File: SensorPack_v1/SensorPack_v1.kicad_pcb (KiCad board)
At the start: 4 copper layers, 53.5 x 50 mm, 31 parts, among them J2 M12x5 A-Type, J3 2x3 Header, J4 M12x5 A-Type, Q1 DMN2310U, U1 STM32C092KCT6, U3 MCP2562-E-SN, U4 TLV7xx_SOT23-5, Y1 8MHz 16pF Load

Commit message: Featured out SensorPack_v1
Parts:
- removed C12: 100nF, Resistor_SMD:R_0603_1608Metric_Pad0.98x0.95mm_HandSolder
- removed C9: 10uF 16V, Capacitor_SMD:C_0805_2012Metric_Pad1.18x1.45mm_HandSolder
- removed D3: 12V TVS 1CH, Diode_SMD:D_SMA
- removed U4: TLV7xx_SOT23-5, Package_TO_SOT_SMD:SOT-23-5
- added C5: 100nF, Resistor_SMD:R_0603_1608Metric_Pad0.98x0.95mm_HandSolder, F.Cu at (132.8, 54.2)
- added C6: 10uF 16V, Capacitor_SMD:C_0805_2012Metric_Pad1.18x1.45mm_HandSolder, F.Cu at (131.8, 66.0)
- added D2: 12V TVS 1CH, Diode_SMD:D_SMA, F.Cu at (140.5, 54.2)
- added J1: M12x5 A-Type, Capstone_Footprints:M12x5_A_Circular_Connector, F.Cu at (148.5, 60.0)
- added J10: 2x3 Pogo Header, Capstone_Footprints:2x03_2.54mm_DIP_pogo, B.Cu at (102.5, 75.0)
- added J5: 4p Header, Connector_PinHeader_2.54mm:PinHeader_1x04_P2.54mm_Vertical, F.Cu at (118.5, 96.7)
- added J6: 4p Header, Connector_PinHeader_2.54mm:PinHeader_1x04_P2.54mm_Vertical, F.Cu at (111.5, 54.0)
- added J7: 4p Header, Connector_PinHeader_2.54mm:PinHeader_1x04_P2.54mm_Vertical, F.Cu at (111.0, 96.7)
- added J8: 6p Header, Connector_PinHeader_2.54mm:PinHeader_1x06_P2.54mm_Vertical, F.Cu at (104.0, 54.0)
- added J9: 4p Header, Connector_PinHeader_2.54mm:PinHeader_1x04_P2.54mm_Vertical, F.Cu at (104.0, 96.5)
- added JP1: Jumper_3_Bridged12, Capstone_Footprints:Jumper_0603_2pos, F.Cu at (128.5, 95.7)
- added JP2: Jumper_3_Bridged12, Capstone_Footprints:Jumper_0603_2pos, F.Cu at (121.0, 95.7)
- added JP3: Jumper_2_Small_Open, Resistor_SMD:R_0603_1608Metric_Pad0.98x0.95mm_HandSolder, F.Cu at (119.0, 64.2)
- added JP4: Jumper_3_Bridged12, Capstone_Footprints:Jumper_0603_2pos, F.Cu at (113.5, 95.7)
- added JP5: Jumper_2_Small_Open, Resistor_SMD:R_0603_1608Metric_Pad0.98x0.95mm_HandSolder, F.Cu at (111.5, 64.2)
- added JP6: Jumper_3_Bridged12, Capstone_Footprints:Jumper_0603_2pos, F.Cu at (106.5, 54.8)
- added R10: 1k, Resistor_SMD:R_0603_1608Metric_Pad0.98x0.95mm_HandSolder, F.Cu at (111.5, 65.8)
- added R11: 2k, Resistor_SMD:R_0603_1608Metric_Pad0.98x0.95mm_HandSolder, F.Cu at (111.5, 67.2)
- added R12: 4k7, Resistor_SMD:R_0603_1608Metric_Pad0.98x0.95mm_HandSolder, F.Cu at (122.3, 115.2)
- added R13: 4k7, Resistor_SMD:R_0603_1608Metric_Pad0.98x0.95mm_HandSolder, F.Cu at (122.3, 117.7)
- added R14: 4k7, Resistor_SMD:R_0603_1608Metric_Pad0.98x0.95mm_HandSolder, F.Cu at (122.3, 120.2)
- added R15: 4k7, Resistor_SMD:R_0603_1608Metric_Pad0.98x0.95mm_HandSolder, F.Cu at (122.3, 122.7)
- added R16: 4k7, Resistor_SMD:R_0603_1608Metric_Pad0.98x0.95mm_HandSolder, F.Cu at (122.3, 125.2)
- added R17: 4k7, Resistor_SMD:R_0603_1608Metric_Pad0.98x0.95mm_HandSolder, F.Cu at (122.3, 127.7)
- added R8: 1k, Resistor_SMD:R_0603_1608Metric_Pad0.98x0.95mm_HandSolder, F.Cu at (119.0, 65.8)
- added R9: 2k, Resistor_SMD:R_0603_1608Metric_Pad0.98x0.95mm_HandSolder, F.Cu at (119.0, 67.2)
- added U2: TLV7xx_SOT23-5, Package_TO_SOT_SMD:SOT-23-5, F.Cu at (130.2, 54.2)
- C1: value 27pF -> 100nF; footprint Capacitor_SMD:C_0603_1608Metric_Pad1.08x0.95mm_HandSolder -> Resistor_SMD:R_0603_1608Metric_Pad0.98x0.95mm_HandSolder
- C3: value 10uF 16V -> 27pF; footprint Capacitor_SMD:C_0805_2012Metric_Pad1.18x1.45mm_HandSolder -> Capacitor_SMD:C_0603_1608Metric_Pad1.08x0.95mm_HandSolder
- C4: value 100nF -> 10uF 16V; footprint Resistor_SMD:R_0603_1608Metric_Pad0.98x0.95mm_HandSolder -> Capacitor_SMD:C_0805_2012Metric_Pad1.18x1.45mm_HandSolder
- CM1: footprint Extra_Footprints:CMChoke_2.6x1.2mm_HandSolder -> Capstone_Footprints:CMChoke_2.6x1.2mm_HandSolder
- J2: footprint Extra_Footprints:M12x5_A_Circular_Connector -> Capstone_Footprints:M12x5_A_Circular_Connector
- J3: value 2x3 Header -> 4p Header; footprint Extra_Footprints:2x03_2.54mm_DIP_pogo -> Connector_PinHeader_2.54mm:PinHeader_1x04_P2.54mm_Vertical; moved to F.Cu
- J4: value M12x5 A-Type -> 4p Header; footprint Extra_Footprints:M12x5_A_Circular_Connector -> Connector_PinHeader_2.54mm:PinHeader_1x04_P2.54mm_Vertical
- LED1: footprint Connector_PinHeader_2.54mm:PinHeader_1x03_P2.54mm_Vertical -> LED_THT:LED_D3.0mm-3
- R1: value 100k -> 4.7k
- R2: value 10R -> 2.2k
- R3: value 10R -> 47k
- R4: value 100k -> 10R
- R5: value 1k -> 10R
- R6: value 1k -> 10k
- R7: value 47k -> 10k
- TH1: value NTC100k B3950 SMT -> NTC10k B3950 SMT
- TH2: value NTC100k B3950 Probe -> NTC10k B3950 Probe
- U1: value STM32C092KCT6 -> MCP2562-E-SN; footprint Package_QFP:LQFP-32_7x7mm_P0.8mm -> Package_SO:SOIC-8_3.9x4.9mm_P1.27mm
- U3: value MCP2562-E-SN -> STM32C092KCT6; footprint Package_SO:SOIC-8_3.9x4.9mm_P1.27mm -> Package_QFP:LQFP-32_7x7mm_P0.8mm
- Y1: footprint Extra_Footprints:Crystal_6x3.5mm -> Capstone_Footprints:Crystal_6x3.5mm
- moved J4 69.2 mm to (119.0, 54.0), turned to 0 degrees
- moved FB1 48.6 mm to (136.2, 54.2), turned to 90 degrees
- moved F1 47.9 mm to (139.5, 57.2)
- moved C8 46.1 mm to (130.2, 57.2), turned to 0 degrees
- moved C4 43.8 mm to (134.5, 54.1), turned to -90 degrees
- moved U3 38.3 mm to (127.0, 75.0), turned to -135 degrees
- moved C3 37.5 mm to (134.8, 71.3), turned to 90 degrees
- moved R6 37.0 mm to (126.5, 59.2), turned to 180 degrees
- moved R7 35.6 mm to (126.3, 67.0), turned to 90 degrees
- moved TH2 34.7 mm to (126.5, 54.0), turned to 0 degrees
- moved TH1 33.9 mm to (127.8, 67.0), turned to -90 degrees
- moved CM1 31.8 mm to (135.2, 96.2), turned to 180 degrees
- moved D1 29.3 mm to (143.3, 96.2), turned to 0 degrees
- moved J3 28.6 mm to (126.0, 96.7)
- moved C7 27.3 mm to (131.8, 69.6), turned to -90 degrees
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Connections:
- C1 pad 1: /OSC+ -> +5V
- C2 pad 1: /OSC- -> /OSC+
- C3 pad 1: +5V -> /OSC-
- C4 pad 1: GND -> +5V
- C4 pad 2: +3V3 -> GND
- C8 pad 1: +5V -> GND
- C8 pad 2: GND -> +3V3
- CM1 pad 2: Net-(U3-CANL) -> Net-(U1-CANL)
- CM1 pad 4: Net-(U3-CANH) -> Net-(U1-CANH)
- J3 pad 1: /SWDIO -> Net-(J3-Pin_1)
- J3 pad 2: /NRST -> GND
- J3 pad 3: GND -> /I2C2_SDA2
- J3 pad 4: GND -> /I2C2_SCL2
- J4 pad 1: +5Vin -> +5V
- J4 pad 2: /CANH -> +3V3
- J4 pad 4: /CANL -> Net-(J4-Pin_4)
- R1 pad 1: /VNTC1 -> /EN_LED_G
- R1 pad 2: GND -> Net-(LED1-K2)
- R2 pad 1: Net-(CM1-Pad3) -> Net-(Q1-D)
- R2 pad 2: /CANH -> Net-(LED1-K1)
- R3 pad 1: Net-(CM1-Pad1) -> +3V3
- R3 pad 2: /CANL -> /EN_LED_R
- R4 pad 1: /VNTC2 -> Net-(CM1-Pad3)
- R4 pad 2: GND -> /CANH
- R5 pad 1: /EN_LED_G -> Net-(CM1-Pad1)
- R5 pad 2: Net-(LED1-K2) -> /CANL
- R6 pad 1: Net-(Q1-D) -> /VNTC1
- R6 pad 2: Net-(LED1-K1) -> GND
- R7 pad 1: +3V3 -> /VNTC2
- R7 pad 2: /EN_LED_R -> GND
- U1 pad 1: /EN_LED_G -> /CAN_TXD
- U1 pad 2: /OSC- -> GND
- U1 pad 3: /OSC+ -> +5V
- U1 pad 4: +3V3 -> /CAN_RXD
- U1 pad 5: GND -> +3V3
- U1 pad 6: /NRST -> Net-(U1-CANL)
- U1 pad 7: /VNTC1 -> Net-(U1-CANH)
- U1 pad 8: /VNTC2 -> /TRANSCEIVER_STBY
- U3 pad 1: /CAN_TXD -> /EN_LED_G
- U3 pad 2: GND -> /OSC-
- U3 pad 3: +5V -> /OSC+
- U3 pad 4: /CAN_RXD -> +3V3
- U3 pad 5: +3V3 -> GND
- U3 pad 6: Net-(U3-CANL) -> /NRST
- U3 pad 7: Net-(U3-CANH) -> /VNTC1
- U3 pad 8: /TRANSCEIVER_STBY -> /VNTC2
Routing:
- net +5V: track 22.6 -> 111.3 mm, vias 1 -> 5
- net GND: track 72.4 -> 30.4 mm, vias 19 -> 79
- net /USART2_RX: track 0.00 -> 34.4 mm
- net /USART2_CK: track 0.00 -> 29.4 mm
- net /SPI1_CS1: track 0.00 -> 28.5 mm
- net /SPI1_SCK: track 0.00 -> 26.3 mm
- net /SPI1_MISO: track 0.00 -> 24.1 mm
- net /USART2_TX: track 0.00 -> 24.0 mm
- net /NRST: track 8.96 -> 32.7 mm
- net /SWDIO: track 4.48 -> 28.2 mm
- net /SWCLK: track 4.48 -> 27.8 mm
- net /SPI1_MOSI: track 0.00 -> 21.8 mm
- net /I2C1_SDA: track 0.00 -> 18.9 mm
- net /I2C1_SCL: track 0.00 -> 17.8 mm
- net /ADC_IN3: track 0.00 -> 17.5 mm
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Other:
- board size 53.5 x 50 mm -> 54 x 50 mm
- board text added: "3V3"
- board text added: "5V"
- board text added: "ADC1"
- board text added: "ADC2"
- board text added: "CLK"
- board text added: "CS"
- board text added: "GND"
- board text added: "I2C1"
- board text added: "I2C2 1"
- board text added: "I2C2 2"
- board text added: "IN"
- board text added: "MISO"
- board text added: "MOSI"
- board text added: "NTC"
- board text added: "PWR"
- board text added: "RX"
- board text added: "SCK"
- board text added: "SCL"
- board text added: "SDA"
- board text added: "SPI1"
- board text added: "TX"
- board text added: "USART"

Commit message: Sensor Pack Update
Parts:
- moved R9 41.4 mm to (126.0, 86.5)
- moved R8 40.4 mm to (126.0, 85.0)
- moved R13 36.4 mm to (118.5, 86.5)
- moved R12 35.4 mm to (118.5, 85.0)
- moved R17 33.1 mm to (111.0, 86.5)
- moved R16 32.2 mm to (111.0, 85.0)
- renumbered R8 to R10, R9 to R11, R14 to R12, R15 to R13, R10 to R14, R11 to R15, R12 to R16, R13 to R17, R16 to R8, R17 to R9
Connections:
- U3 pad 18: /GP_PA8 -> unconnected-(U3-PA8-Pad18)
- U3 pad 20: /GP_PA15 -> unconnected-(U3-PC6-Pad20)
- U3 pad 26: /GP_PA15 -> unconnected-(U3-PA15-Pad26)
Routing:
- net /GP_PA15: track 7.00 -> 0.00 mm
- net +3V3: track 17.0 -> 21.5 mm, vias 10 -> 13
- net /I2C1_SDA: track 18.9 -> 21.8 mm
- net /I2C1_SCL: track 17.8 -> 19.5 mm
- net GND: vias 79 -> 78

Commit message: Final changes to Sensor Pack
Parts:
- added H1: M3 Bolt, MountingHole:MountingHole_3.2mm_M3, F.Cu at (110.0, 75.0)
- added TP1: 1p, Connector_PinHeader_2.54mm:PinHeader_1x01_P2.54mm_Vertical, F.Cu at (141.0, 62.8)
- added TP2: 1p, Connector_PinHeader_2.54mm:PinHeader_1x01_P2.54mm_Vertical, F.Cu at (137.2, 62.8)
- F1: value 200mA Polyfuse -> 1A Polyfuse
- J1: value M12x5 A-Type -> M12x5 A-Type Female; footprint Capstone_Footprints:M12x5_A_Circular_Connector -> Capstone_Footprints:M12A05PFFRSF7003
- J10: footprint Capstone_Footprints:2x03_2.54mm_DIP_pogo -> Connector_PinHeader_2.54mm:PinHeader_2x03_P2.54mm_Vertical; moved to F.Cu
- J2: value M12x5 A-Type -> M12x5 A-Type Male; footprint Capstone_Footprints:M12x5_A_Circular_Connector -> Capstone_Footprints:M12A05PMMRSF7003
- R1: value 4.7k -> 4k7
- moved J10 2.85 mm to (103.8, 77.5), turned to 180 degrees
- moved J2 2.50 mm to (146.7, 88.2), turned to 90 degrees
- moved J1 2.48 mm to (146.8, 58.2), turned to 90 degrees
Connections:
- J10 pad 2: /NRST -> /SWCLK
- J10 pad 3: GND -> /NRST
- J10 pad 4: GND -> +3V3
- J10 pad 5: +3V3 -> GND
- J10 pad 6: /SWCLK -> GND
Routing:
- net /CANL: track 46.4 -> 56.0 mm
- net +3V3: track 21.5 -> 28.6 mm, vias 13 -> 12
- net /SWDIO: track 28.2 -> 24.6 mm
- net /NRST: track 32.7 -> 30.1 mm
- net /SWCLK: track 27.8 -> 30.3 mm
- net /CANH: track 39.9 -> 41.1 mm
- net +5Vin: track 40.9 -> 40.3 mm
- net GND: vias 78 -> 79
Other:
- board size 54 x 50 mm -> 58 x 50 mm
- board text added: "VITAL Capstone Vector Drive Sensor Core Rev. 1.0"

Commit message: BOM changes, minor schematic change
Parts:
- removed Q1: DMN2310U, Package_TO_SOT_SMD:SOT-23-3
- added Q2: DMP2045U-7, Capstone_Footprints:SOT-23-3, F.Cu at (142.2, 75.8)
- R1: value 4k7 -> 1k
- R2: value 2.2k -> 330R
- Y1: value 8MHz 16pF Load -> 8MHz 18pF Load
- moved R1 1.82 mm to (142.8, 73.2)
- moved R2 1.36 mm to (142.8, 71.8)
- moved LED1 0.25 mm to (146.8, 77.5)
- moved R3 0.10 mm to (142.5, 78.2), turned to 180 degrees
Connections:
- LED1 pad 1: Net-(LED1-K1) -> Net-(LED1-A1)
- LED1 pad 2: +5V -> GND
- LED1 pad 3: Net-(LED1-K2) -> Net-(LED1-A2)
- R1 pad 1: /EN_LED_G -> Net-(Q2-S)
- R1 pad 2: Net-(LED1-K2) -> Net-(LED1-A1)
- R2 pad 1: Net-(Q1-D) -> /EN_LED_G
- R2 pad 2: Net-(LED1-K1) -> Net-(LED1-A2)
- R3 pad 1: +3V3 -> /EN_LED_R
- R3 pad 2: /EN_LED_R -> GND
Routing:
- net Net-(LED1-K1): track 5.80 -> 0.00 mm
- net Net-(LED1-A1): track 0.00 -> 5.57 mm
- net +5V: track 111.3 -> 107.2 mm
- net Net-(LED1-K2): track 3.60 -> 0.00 mm
- net Net-(LED1-A2): track 0.00 -> 3.38 mm
- net Net-(Q1-D): track 3.02 -> 0.00 mm
- net Net-(Q2-S): track 0.00 -> 2.80 mm
- net /EN_LED_R: track 14.3 -> 13.7 mm
- net GND: vias 79 -> 78

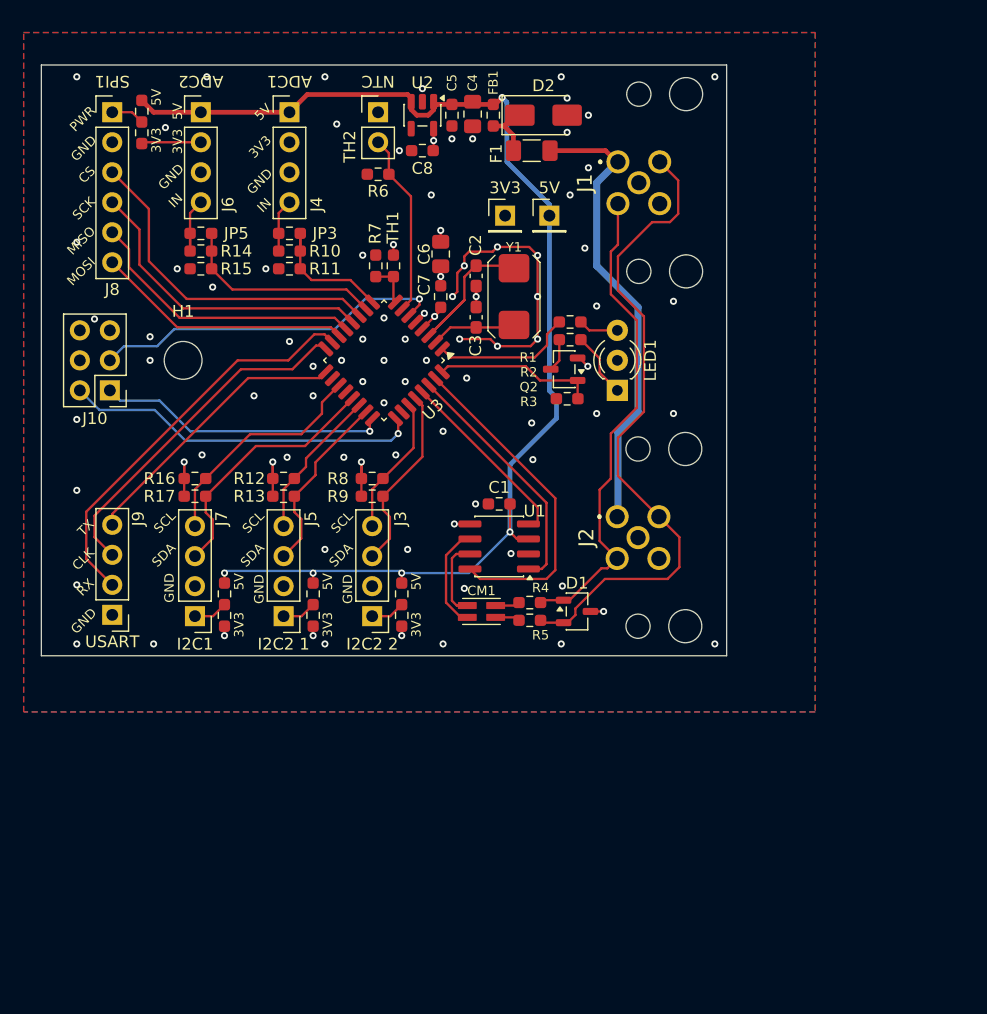
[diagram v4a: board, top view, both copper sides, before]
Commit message: Added some mechanical notes, adjusted traces to not run under bolt (just in case), scooted top connector back in place
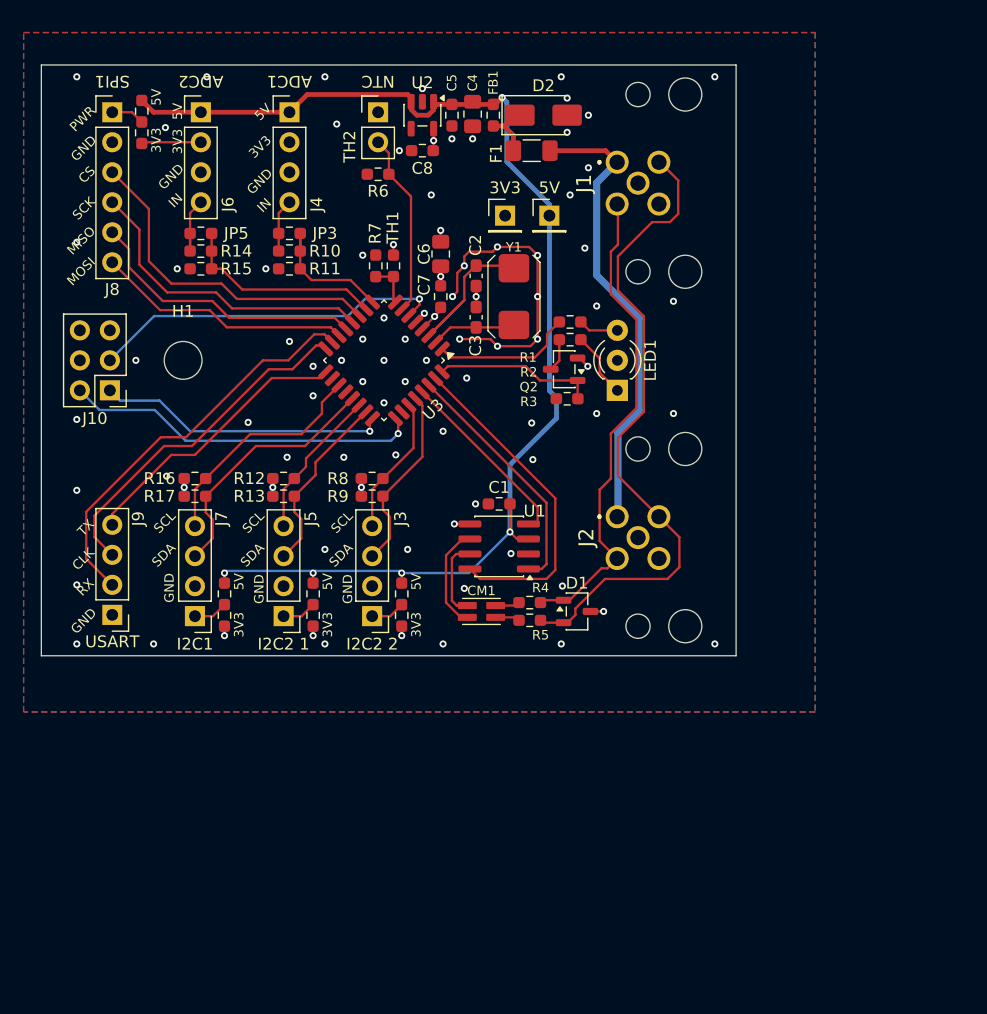
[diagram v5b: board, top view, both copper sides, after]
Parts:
- moved J1 0.08 mm to (146.7, 58.2)
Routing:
- net +3V3: track 29.0 -> 20.6 mm
- net GND: vias 78 -> 75
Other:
- board size 58 x 50 mm -> 58.8 x 50 mm
- board text added: "M3 Bolt"

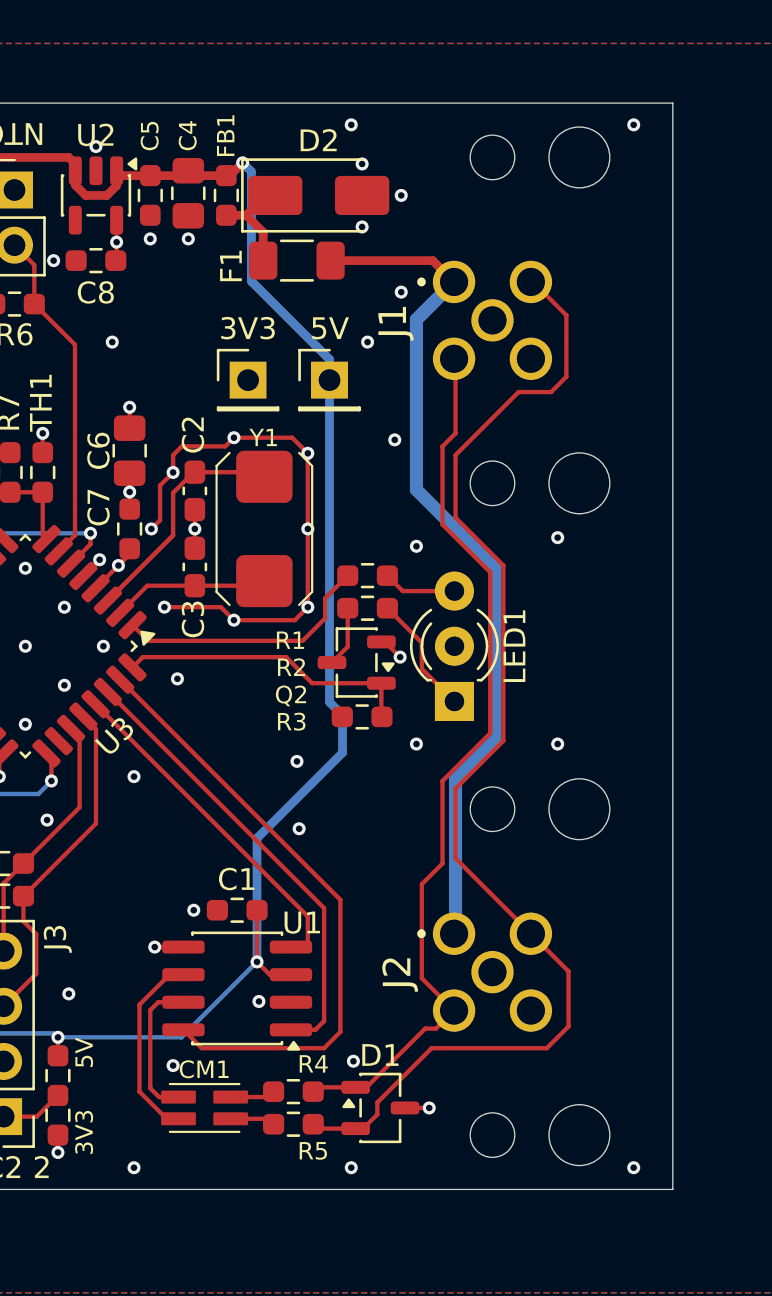
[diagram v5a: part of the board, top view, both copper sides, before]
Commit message: Connectors too close to edge, changed connector spacing, rearranged components appropriately
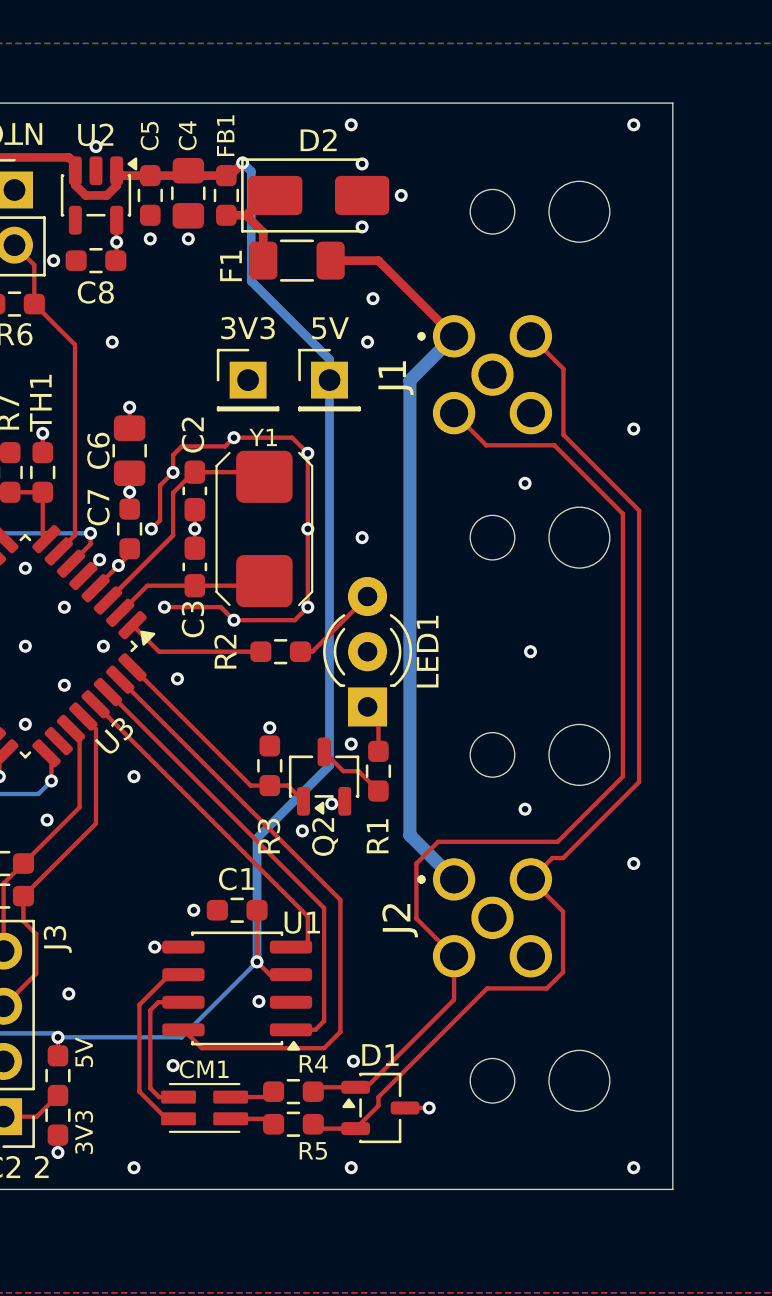
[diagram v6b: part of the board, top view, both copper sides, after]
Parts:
- moved R1 7.52 mm to (143.2, 80.8), turned to 90 degrees
- moved Q2 5.46 mm to (140.8, 81.0), turned to 90 degrees
- moved R2 5.32 mm to (138.8, 75.2)
- moved R3 4.81 mm to (138.2, 80.5), turned to 90 degrees
- moved LED1 4.01 mm to (142.8, 77.8)
- moved J1 2.50 mm to (146.7, 60.7)
- moved J2 2.50 mm to (146.7, 85.7)
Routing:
- net /CANH: track 41.1 -> 48.2 mm
- net /CANL: track 56.0 -> 49.1 mm
- net +5Vin: track 40.4 -> 33.8 mm
- net /EN_LED_G: track 12.0 -> 6.41 mm
- net Net-(LED1-A1): track 5.57 -> 2.25 mm
- net /EN_LED_R: track 13.7 -> 10.4 mm
- net Net-(LED1-A2): track 3.38 -> 4.14 mm
- net +3V3: track 20.6 -> 20.1 mm
- net GND: vias 75 -> 77
